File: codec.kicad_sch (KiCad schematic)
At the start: 13 parts, among them U7 TLV320AIC3100

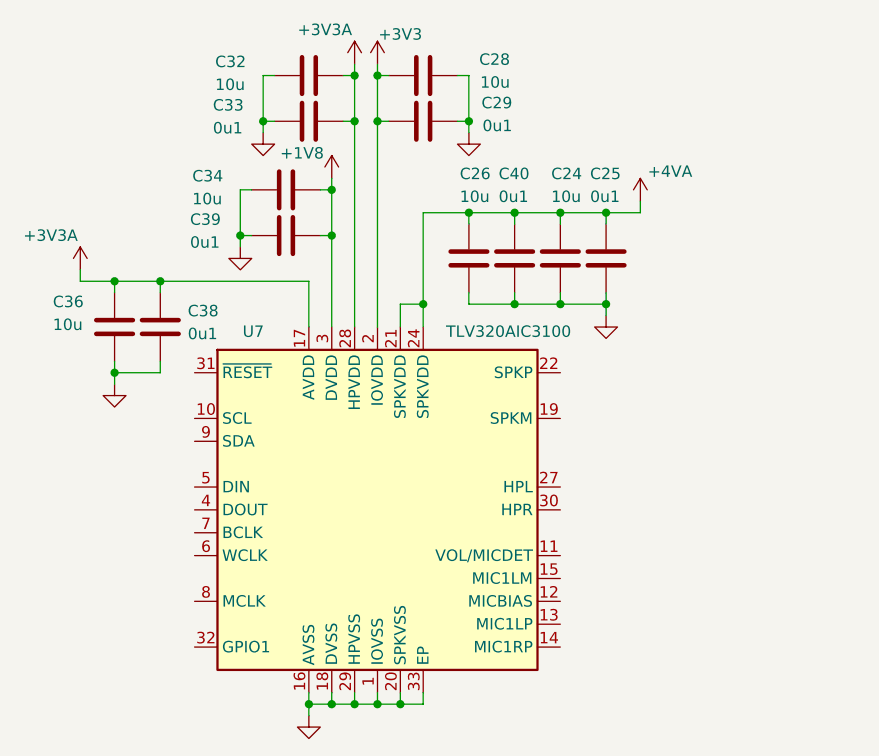
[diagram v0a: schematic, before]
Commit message: schem: remove "extra" 0u1 capacitors from codec
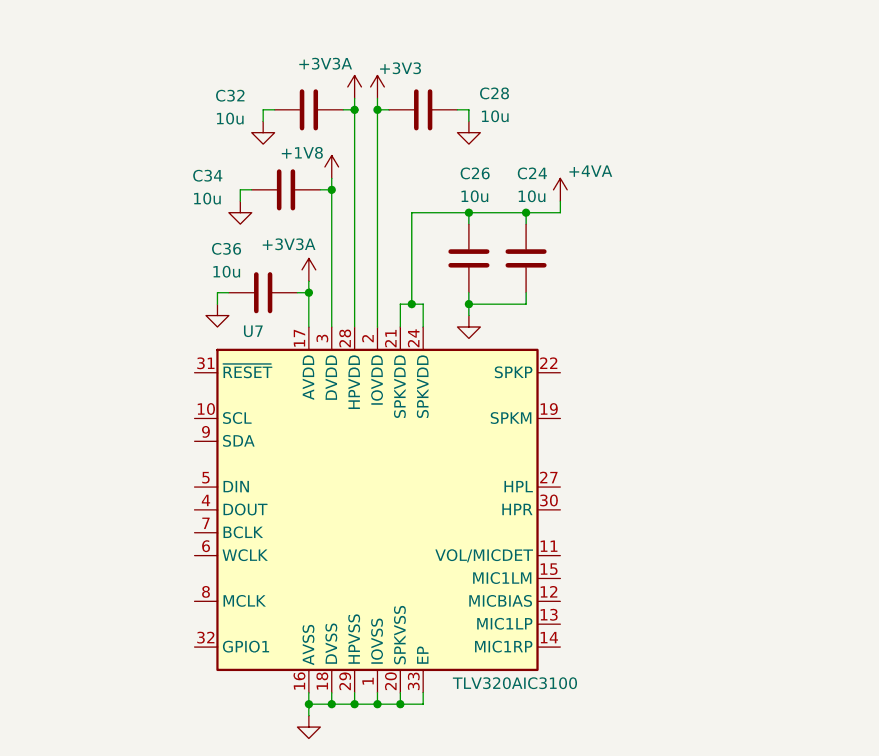
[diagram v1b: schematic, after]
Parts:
- removed C25, C29, C33, C38, C39, C40: 0u1, Capacitor_SMD:C_0402_1005Metric, symbol Device:C
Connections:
- net +3V3A: now also C36.2; no longer C36.1
- net GND: now also C36.1; no longer C36.2
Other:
- moved on the sheet: C24, C28, C32

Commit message: schem: add codec surrounding circuitery
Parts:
- added C25, C27: 10u, Capacitor_SMD:C_0805_2012Metric, symbol Device:C_Small
- added C29: 0u1, Capacitor_SMD:C_0402_1005Metric, symbol Device:C
- added J1: AudioJack4, symbol Connector_Audio:AudioJack4
- added J8: Conn_01x02, Connector_JST:JST_PH_B2B-PH-K_1x02_P2.00mm_Vertical, symbol Device:Speaker
- added MK1: Microphone, Connector_JST:JST_PH_B2B-PH-K_1x02_P2.00mm_Vertical, symbol Device:Microphone
- added R26: 2k2, Resistor_SMD:R_0402_1005Metric, symbol Device:R_Small
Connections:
- net GND: now also J1.R2, MK1.1 (-)
- net SCL: now reaches U7.10 (SCL)
- net at U7.11 (VOL/MICDET): now also C29.2, J1.S, MK1.2 (+), R26.2
- net at U7.12 (MICBIAS): now also R26.1
- net at U7.14 (MIC1RP): now also C29.1
- net at U7.19 (SPKM), U7.23 (SPKM): now also J8.2
- net at U7.22 (SPKP), U7.26 (SPKP): now also J8.1
- net at U7.27 (HPL): now also C25.1
- net at U7.30 (HPR): now also C27.1
- net ~{RESET}: now reaches U7.31 (~{RESET})
- net GPIO1: now reaches U7.32 (GPIO1)
- net DOUT: now reaches U7.4 (DOUT)
- net DIN: now reaches U7.5 (DIN)
- net WCLK: now reaches U7.6 (WCLK)
- net BCLK: now reaches U7.7 (BCLK)
- net MCLK: now reaches U7.8 (MCLK)
- net SDA: now reaches U7.9 (SDA)
- new net: C27.2, J1.R1
- new net: C25.2, J1.T
- no-connect marks 0 -> 2
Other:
- note added: "4W"

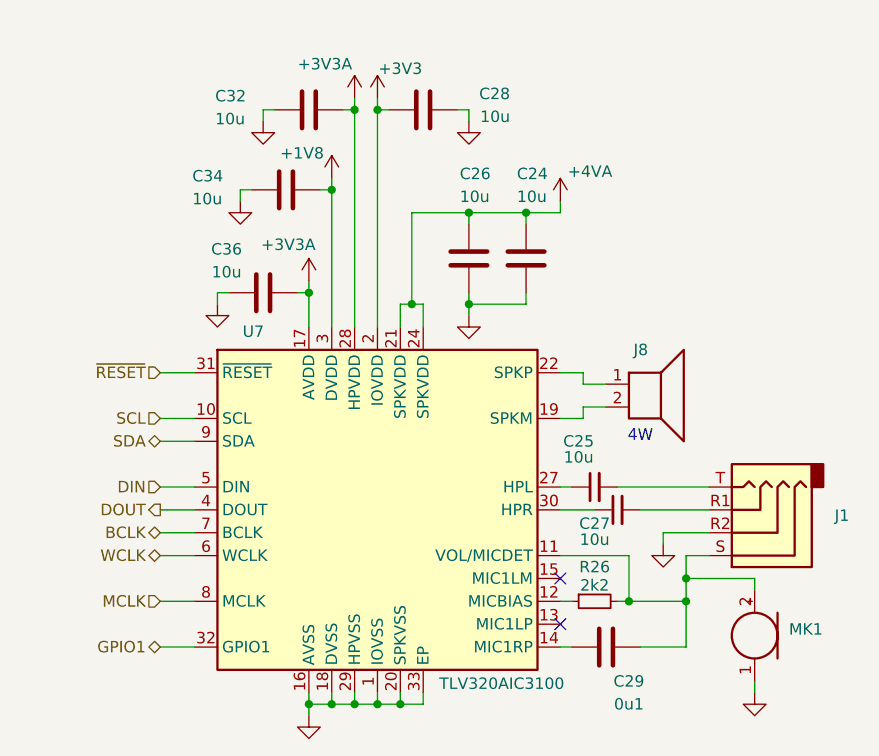
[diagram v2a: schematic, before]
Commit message: schem: add hierarchical line output labels to codec
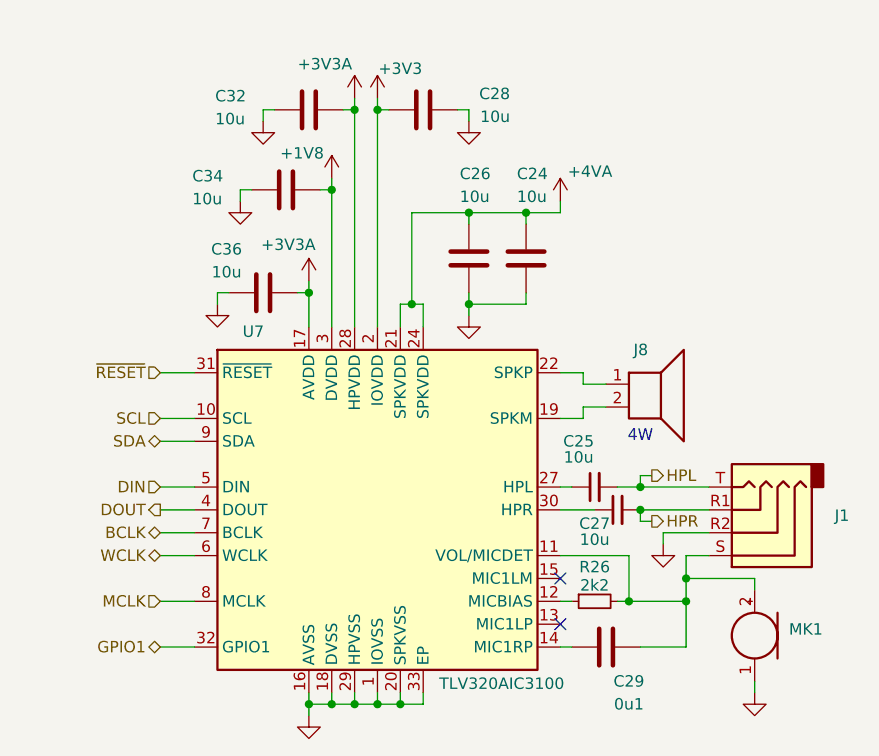
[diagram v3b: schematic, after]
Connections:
- net HPR: now reaches C27.2, J1.R1
- net HPL: now reaches C25.2, J1.T
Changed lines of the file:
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@@
+	)
+	(junction
+		(at 176.53 105.41)
+		(diameter 0)
+		(color 0 0 0 0)
 	)
 	(junction
@@
 	(junction
 		(at 139.7 127)
+		(diameter 0)
+		(color 0 0 0 0)
+	)
+	(junction
+		(at 176.53 102.87)
 		(diameter 0)
 		(color 0 0 0 0)
@@
 	(wire
 		(pts
+			(xy 176.53 101.6) (xy 176.53 102.87)
+		)
+		(stroke
+			(width 0)
+			(type default)
+		)
+	)
+	(wire
+		(pts
 			(xy 163.83 72.39) (xy 167.64 72.39)
 		)
@@
 	(wire
 		(pts
+			(xy 176.53 102.87) (xy 184.15 102.87)
+		)
+		(stroke
+			(width 0)
+			(type default)
+		)
+	)
+	(wire
+		(pts
 			(xy 175.26 115.57) (xy 181.61 115.57)
 		)
@@
 	(wire
 		(pts
-			(xy 173.99 102.87) (xy 184.15 102.87)
+			(xy 173.99 102.87) (xy 176.53 102.87)
 		)
 		(stroke
@@
 	(wire
 		(pts
+			(xy 176.53 106.68) (xy 176.53 105.41)
+		)
+		(stroke
+			(width 0)
+			(type default)
+		)
+	)
+	(wire
+		(pts
 			(xy 147.32 127) (xy 149.86 127)
 		)
@@
 		(pts
 			(xy 144.78 59.69) (xy 144.78 60.96)
+		)
+		(stroke
+			(width 0)
+			(type default)
+		)
+	)
+	(wire
+		(pts
+			(xy 177.8 106.68) (xy 176.53 106.68)
+		)
+		(stroke
+			(width 0)
+			(type default)
+		)
+	)
+	(wire
+		(pts
+			(xy 176.53 101.6) (xy 177.8 101.6)
 		)
 		(stroke
@@
 		)
 	)
+	(hierarchical_label "HPL"
+		(shape output)
+		(at 177.8 101.6 0)
+		(effects
+			(font
+				(size 1.27 1.27)
+			)
+			(justify left)
+		)
+	)
 	(hierarchical_label "GPIO1"
 		(shape bidirectional)
@@
 		)
 	)
+	(hierarchical_label "HPR"
+		(shape output)
+		(at 177.8 106.68 0)
+		(effects
+			(font
+				(size 1.27 1.27)
+			)
+			(justify left)
+		)
+	)

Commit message: schem: add missing footprints
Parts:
- J1: footprint (none) -> Connector_Audio:Jack_3.5mm_KoreanHropartsElec_PJ-320D-4A_Horizontal; Basic (none) -> X; JLCPCB Part # (none) -> C431535; Manufacturer (none) -> Shou HAN; Manufacturer Part Number (none) -> PJ-320D
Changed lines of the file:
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@@
 			)
 		)
-		(property "Footprint" ""
+		(property "Footprint" "Connector_Audio:Jack_3.5mm_KoreanHropartsElec_PJ-320D-4A_Horizontal"
 			(at 189.23 107.95 0)
 			(hide yes)
@@
 			(at 189.23 107.95 0)
 			(hide yes)
+			(show_name no)
+			(do_not_autoplace no)
+			(effects
+				(font
+					(size 1.27 1.27)
+				)
+			)
+		)
+		(property "Basic" "X"
+			(at 189.23 107.95 0)
+			(hide yes)
+			(show_name no)
+			(do_not_autoplace no)
+			(effects
+				(font
+					(size 1.27 1.27)
+				)
+			)
+		)
+		(property "JLCPCB Part #" "C431535"
+			(at 189.23 107.95 0)
+			(hide yes)
+			(show_name no)
+			(do_not_autoplace no)
+			(effects
+				(font
+					(size 1.27 1.27)
+				)
+			)
+		)
+		(property "Manufacturer" "Shou HAN"
+			(at 189.23 107.95 0)
+			(hide yes)
+			(show_name no)
+			(do_not_autoplace no)
+			(effects
+				(font
+					(size 1.27 1.27)
+				)
+			)
+		)
+		(property "Manufacturer Part Number" "PJ-320D"
+			(at 189.23 107.95 0)
+			(hide yes)

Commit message: schem: add ordering info to BOM
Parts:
- C25, C27: JLCPCB Part # C16780 -> C440198; Manufacturer Samsung Electro-Mechanics -> Murata; Manufacturer Part Number CL21A476MQYNNNE -> GRM21BR61H106KE43L
- U7: Basic (none) -> X; JLCPCB Part # (none) -> C478458; Manufacturer (none) -> Texas Instruments; Manufacturer Part Number (none) -> TLV320AIC3100IRHBR
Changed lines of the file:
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@@
 			)
 		)
-		(property "Manufacturer" "Samsung Electro-Mechanics "
+		(property "Manufacturer" "Murata"
 			(at 173.99 105.41 0)
 			(hide yes)
@@
 			)
 		)
-		(property "Manufacturer Part Number" "CL21A476MQYNNNE"
+		(property "Manufacturer Part Number" "GRM21BR61H106KE43L"
 			(at 173.99 105.41 0)
 			(hide yes)
@@
 			)
 		)
-		(property "JLCPCB Part #" "C16780"
+		(property "JLCPCB Part #" "C440198"
 			(at 173.99 105.41 0)
 			(hide yes)
@@
 		)
 		(property "Description" "Low Power Audio Codec with Audio Processing and Mono Class‑D Amplifier, VQFN-32"
+			(at 147.32 105.41 0)
+			(hide yes)
+			(show_name no)
+			(do_not_autoplace no)
+			(effects
+				(font
+					(size 1.27 1.27)
+				)
+			)
+		)
+		(property "Basic" "X"
+			(at 147.32 105.41 0)
+			(hide yes)
+			(show_name no)
+			(do_not_autoplace no)
+			(effects
+				(font
+					(size 1.27 1.27)
+				)
+			)
+		)
+		(property "JLCPCB Part #" "C478458"
+			(at 147.32 105.41 0)
+			(hide yes)
+			(show_name no)
+			(do_not_autoplace no)
+			(effects
+				(font
+					(size 1.27 1.27)
+				)
+			)
+		)
+		(property "Manufacturer" "Texas Instruments"
+			(at 147.32 105.41 0)
+			(hide yes)
+			(show_name no)
+			(do_not_autoplace no)
+			(effects
+				(font
+					(size 1.27 1.27)
+				)
+			)
+		)
+		(property "Manufacturer Part Number" "TLV320AIC3100IRHBR"
 			(at 147.32 105.41 0)
 			(hide yes)
@@
 			)
 		)
-		(property "Manufacturer" "Samsung Electro-Mechanics "
+		(property "Manufacturer" "Murata"
 			(at 171.45 102.87 0)
 			(hide yes)
@@
 			)
 		)
-		(property "Manufacturer Part Number" "CL21A476MQYNNNE"
+		(property "Manufacturer Part Number" "GRM21BR61H106KE43L"
 			(at 171.45 102.87 0)
 			(hide yes)
@@
 			)
 		)
-		(property "JLCPCB Part #" "C16780"
+		(property "JLCPCB Part #" "C440198"
 			(at 171.45 102.87 0)
 			(hide yes)

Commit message: schem: add title
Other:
- company: (none) -> Rémi Ait-Younes
- title: (none) -> S6TM Stereo Dev 1
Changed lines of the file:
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@@
 	(generator_version "10.0")
 	(paper "A4")
+	(title_block
+		(title "S6TM Stereo Dev 1")
+		(date "2026-04-11")
+		(rev "01")
+		(company "Rémi Ait-Younes")
+	)
 	(text "4W"
 		(exclude_from_sim no)

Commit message: schem: reannotate
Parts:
- renumbered C36 to C15, C34 to C16, C32 to C17, C28 to C18, C26 to C19, C24 to C20, C25 to C21, C29 to C22, C27 to C23, J8 to J4, J1 to J5, R26 to R31, U7 to U3
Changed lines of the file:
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@@
 		(in_pos_files yes)
 		(dnp no)
-		(property "Reference" "#PWR079"
+		(property "Reference" "#PWR068"
 			(at 189.23 132.08 0)
 			(hide yes)
@@
 			(project "s6tm-stereo-dev-1"
 				(path "/41fad0d7-0cae-453e-a16c-bdf8be036e99/4cb8bb37-39af-4125-bddf-edec04b213be"
-					(reference "#PWR079")
+					(reference "#PWR068")
 					(unit 1)
 				)
@@
 		(in_pos_files yes)
 		(dnp no)
-		(property "Reference" "#PWR072"
+		(property "Reference" "#PWR058"
 			(at 134.62 68.58 0)
 			(hide yes)
@@
 			(project "s6tm-stereo-dev-1"
 				(path "/41fad0d7-0cae-453e-a16c-bdf8be036e99/4cb8bb37-39af-4125-bddf-edec04b213be"
-					(reference "#PWR072")
+					(reference "#PWR058")
 					(unit 1)
 				)
@@
 		(in_pos_files yes)
 		(dnp no)
-		(property "Reference" "C34"
+		(property "Reference" "C16"
 			(at 126.746 68.326 90)
 			(show_name no)
@@
 			(project "s6tm-stereo-dev-1"
 				(path "/41fad0d7-0cae-453e-a16c-bdf8be036e99/4cb8bb37-39af-4125-bddf-edec04b213be"
-					(reference "C34")
+					(reference "C16")
 					(unit 1)
 				)
@@
 		(in_pos_files yes)
 		(dnp no)
-		(property "Reference" "#PWR066"
+		(property "Reference" "#PWR064"
 			(at 157.48 68.58 0)
 			(hide yes)
@@
 			(project "s6tm-stereo-dev-1"
 				(path "/41fad0d7-0cae-453e-a16c-bdf8be036e99/4cb8bb37-39af-4125-bddf-edec04b213be"
-					(reference "#PWR066")
+					(reference "#PWR064")
 					(unit 1)
 				)
@@
 		(in_pos_files yes)
 		(dnp no)
-		(property "Reference" "C26"
+		(property "Reference" "C19"
 			(at 156.464 68.072 0)
 			(show_name no)
@@
 			(project "s6tm-stereo-dev-1"
 				(path "/41fad0d7-0cae-453e-a16c-bdf8be036e99/4cb8bb37-39af-4125-bddf-edec04b213be"
-					(reference "C26")
+					(reference "C19")
 					(unit 1)
 				)
@@
 		(in_pos_files yes)
 		(dnp no)
-		(property "Reference" "J1"
+		(property "Reference" "J5"
 			(at 198.12 106.0451 0)
 			(show_name no)
@@
 			(project "s6tm-stereo-dev-1"
 				(path "/41fad0d7-0cae-453e-a16c-bdf8be036e99/4cb8bb37-39af-4125-bddf-edec04b213be"
-					(reference "J1")
+					(reference "J5")
 					(unit 1)
 				)
@@
 		(in_pos_files yes)
 		(dnp no)
-		(property "Reference" "C27"
+		(property "Reference" "C23"
 			(at 171.45 106.934 90)
 			(show_name no)
@@
 			(project "s6tm-stereo-dev-1"
 				(path "/41fad0d7-0cae-453e-a16c-bdf8be036e99/4cb8bb37-39af-4125-bddf-edec04b213be"
-					(reference "C27")
+					(reference "C23")
 					(unit 1)
 				)
@@
 		(in_pos_files yes)
 		(dnp no)
-		(property "Reference" "U7"
+		(property "Reference" "U3"
 			(at 132.334 85.598 0)
 			(show_name no)
@@
 			(project "s6tm-stereo-dev-1"
 				(path "/41fad0d7-0cae-453e-a16c-bdf8be036e99/4cb8bb37-39af-4125-bddf-edec04b213be"
-					(reference "U7")
+					(reference "U3")
 					(unit 1)
 				)
@@
 		(in_pos_files yes)
 		(dnp no)
-		(property "Reference" "#PWR076"
+		(property "Reference" "#PWR056"
 			(at 129.54 88.9 0)
 			(hide yes)
@@
 			(project "s6tm-stereo-dev-1"
 				(path "/41fad0d7-0cae-453e-a16c-bdf8be036e99/4cb8bb37-39af-4125-bddf-edec04b213be"
-					(reference "#PWR076")
+					(reference "#PWR056")
 					(unit 1)
 				)
@@
 		(in_pos_files yes)
 		(dnp no)
-		(property "Reference" "C32"
+		(property "Reference" "C17"
 			(at 129.286 59.436 90)
 			(show_name no)
@@
 			(project "s6tm-stereo-dev-1"
 				(path "/41fad0d7-0cae-453e-a16c-bdf8be036e99/4cb8bb37-39af-4125-bddf-edec04b213be"
-					(reference "C32")
+					(reference "C17")
 					(unit 1)
 				)
@@
 		(in_pos_files yes)
 		(dnp no)
-		(property "Reference" "#PWR03"
+		(property "Reference" "#PWR066"
 			(at 167.64 74.93 0)
 			(hide yes)
@@
 			(project "s6tm-stereo-dev-1"
 				(path "/41fad0d7-0cae-453e-a16c-bdf8be036e99/4cb8bb37-39af-4125-bddf-edec04b213be"
-					(reference "#PWR03")
+					(reference "#PWR066")
 					(unit 1)
 				)
@@
 		(in_pos_files yes)
 		(dnp no)
-		(property "Reference" "#PWR077"
+		(property "Reference" "#PWR060"
 			(at 139.7 134.62 0)
 			(hide yes)
@@
 			(project "s6tm-stereo-dev-1"
 				(path "/41fad0d7-0cae-453e-a16c-bdf8be036e99/4cb8bb37-39af-4125-bddf-edec04b213be"
-					(reference "#PWR077")
+					(reference "#PWR060")
 					(unit 1)
 				)
@@
 		(in_pos_files yes)
 		(dnp no)
-		(property "Reference" "#PWR074"
+		(property "Reference" "#PWR057"
 			(at 132.08 77.47 0)
 			(hide yes)
@@
 			(project "s6tm-stereo-dev-1"
 				(path "/41fad0d7-0cae-453e-a16c-bdf8be036e99/4cb8bb37-39af-4125-bddf-edec04b213be"
-					(reference "#PWR074")
+					(reference "#PWR057")
 					(unit 1)
 				)
@@
 		(in_pos_files yes)
 		(dnp no)
-		(property "Reference" "#PWR056"
+		(property "Reference" "#PWR065"
 			(at 157.48 90.17 0)
 			(hide yes)
@@
 			(project "s6tm-stereo-dev-1"
 				(path "/41fad0d7-0cae-453e-a16c-bdf8be036e99/4cb8bb37-39af-4125-bddf-edec04b213be"
-					(reference "#PWR056")
+					(reference "#PWR065")
 					(unit 1)
 				)
@@
 		(in_pos_files yes)
 		(dnp no)
-		(property "Reference" "#PWR065"
+		(property "Reference" "#PWR063"
 			(at 147.32 63.5 0)
 			(hide yes)
@@
 			(project "s6tm-stereo-dev-1"
 				(path "/41fad0d7-0cae-453e-a16c-bdf8be036e99/4cb8bb37-39af-4125-bddf-edec04b213be"
-					(reference "#PWR065")
+					(reference "#PWR063")
 					(unit 1)
 				)
@@
 		(in_pos_files yes)
 		(dnp no)
-		(property "Reference" "#PWR04"
+		(property "Reference" "#PWR061"
 			(at 142.24 72.39 0)
 			(hide yes)
@@
 			(project "s6tm-stereo-dev-1"
 				(path "/41fad0d7-0cae-453e-a16c-bdf8be036e99/4cb8bb37-39af-4125-bddf-edec04b213be"
-					(reference "#PWR04")
+					(reference "#PWR061")
 					(unit 1)
 				)
@@
 		(in_pos_files yes)
 		(dnp no)
-		(property "Reference" "C28"
+		(property "Reference" "C18"
 			(at 162.052 59.182 90)
 			(show_name no)
@@
 			(project "s6tm-stereo-dev-1"
 				(path "/41fad0d7-0cae-453e-a16c-bdf8be036e99/4cb8bb37-39af-4125-bddf-edec04b213be"
-					(reference "C28")
+					(reference "C18")
 					(unit 1)
 				)
@@
 		(in_pos_files yes)
 		(dnp no)
-		(property "Reference" "#PWR078"
+		(property "Reference" "#PWR067"
 			(at 179.07 115.57 0)
 			(hide yes)
@@
 			(project "s6tm-stereo-dev-1"
 				(path "/41fad0d7-0cae-453e-a16c-bdf8be036e99/4cb8bb37-39af-4125-bddf-edec04b213be"
-					(reference "#PWR078")
+					(reference "#PWR067")
 					(unit 1)
 				)
@@
 		(in_pos_files yes)
 		(dnp no)
-		(property "Reference" "J8"
+		(property "Reference" "J4"
 			(at 175.768 87.63 0)
 			(show_name no)
@@
 			(project "s6tm-stereo-dev-1"
 				(path "/41fad0d7-0cae-453e-a16c-bdf8be036e99/4cb8bb37-39af-4125-bddf-edec04b213be"
-					(reference "J8")
+					(reference "J4")
 					(unit 1)
 				)
@@
 		(in_pos_files yes)
 		(dnp no)
-		(property "Reference" "#PWR075"
+		(property "Reference" "#PWR059"
 			(at 139.7 83.82 0)
 			(hide yes)
@@
 			(project "s6tm-stereo-dev-1"
 				(path "/41fad0d7-0cae-453e-a16c-bdf8be036e99/4cb8bb37-39af-4125-bddf-edec04b213be"
-					(reference "#PWR075")
+					(reference "#PWR059")
 					(unit 1)
 				)
@@
 		(in_pos_files yes)
 		(dnp no)
-		(property "Reference" "C36"
+		(property "Reference" "C15"
 			(at 130.556 76.454 90)
 			(show_name no)
@@
 			(project "s6tm-stereo-dev-1"
 				(path "/41fad0d7-0cae-453e-a16c-bdf8be036e99/4cb8bb37-39af-4125-bddf-edec04b213be"
-					(reference "C36")
+					(reference "C15")
 					(unit 1)
 				)
@@
 		(in_pos_files yes)
 		(dnp no)
-		(property "Reference" "C24"
+		(property "Reference" "C20"
 			(at 162.814 68.072 0)
 			(show_name no)
@@
 			(project "s6tm-stereo-dev-1"
 				(path "/41fad0d7-0cae-453e-a16c-bdf8be036e99/4cb8bb37-39af-4125-bddf-edec04b213be"
-					(reference "C24")
+					(reference "C20")
 					(unit 1)
 				)
@@
 		(in_pos_files yes)
 		(dnp no)
-		(property "Reference" "C25"
+		(property "Reference" "C21"
 			(at 169.672 97.79 90)
 			(show_name no)
@@
 			(project "s6tm-stereo-dev-1"
 				(path "/41fad0d7-0cae-453e-a16c-bdf8be036e99/4cb8bb37-39af-4125-bddf-edec04b213be"
-					(reference "C25")
+					(reference "C21")
 					(unit 1)
 				)
@@
 		(in_pos_files yes)
 		(dnp no)
-		(property "Reference" "R26"
+		(property "Reference" "R31"
 			(at 171.45 111.76 90)
 			(show_name no)
@@
 			(project "s6tm-stereo-dev-1"
 				(path "/41fad0d7-0cae-453e-a16c-bdf8be036e99/4cb8bb37-39af-4125-bddf-edec04b213be"
-					(reference "R26")
+					(reference "R31")
 					(unit 1)
 				)
@@
 		(in_pos_files yes)
 		(dnp no)
-		(property "Reference" "C29"
+		(property "Reference" "C22"
 			(at 175.26 124.46 90)
 			(show_name no)
@@
 			(project "s6tm-stereo-dev-1"
 				(path "/41fad0d7-0cae-453e-a16c-bdf8be036e99/4cb8bb37-39af-4125-bddf-edec04b213be"
-					(reference "C29")
+					(reference "C22")
 					(unit 1)
 				)
@@
 		(in_pos_files yes)
 		(dnp no)
-		(property "Reference" "#PWR073"
+		(property "Reference" "#PWR062"
 			(at 144.78 63.5 0)
 			(hide yes)
@@
 			(project "s6tm-stereo-dev-1"
 				(path "/41fad0d7-0cae-453e-a16c-bdf8be036e99/4cb8bb37-39af-4125-bddf-edec04b213be"
-					(reference "#PWR073")
+					(reference "#PWR062")
 					(unit 1)
 				)
